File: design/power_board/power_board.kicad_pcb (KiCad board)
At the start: 2 copper layers, 68.5 x 38.5 mm, 48 parts, among them J1 Screw_Terminal_01x02, J2 Screw_Terminal_01x02, J3 Screw_Terminal_01x03, U1 LMR14050, U2 LT3045-1, U3 LT3045-1

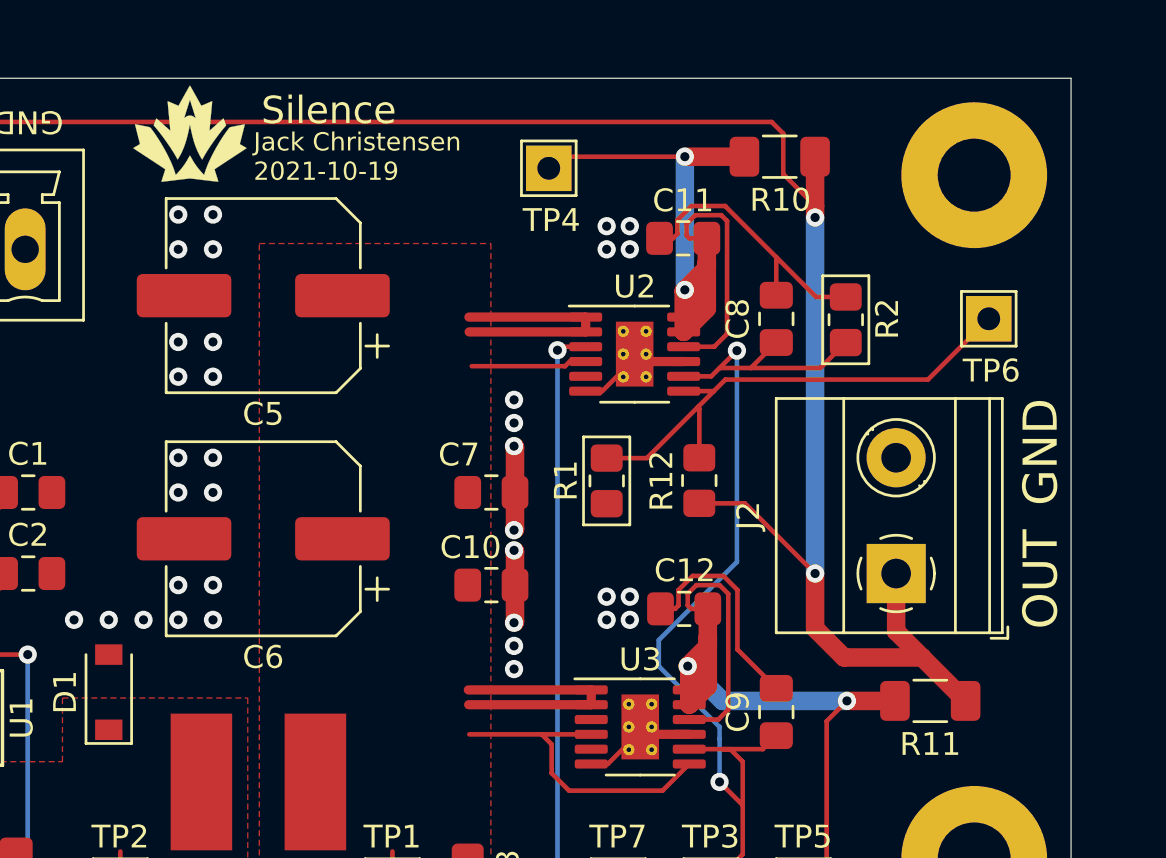
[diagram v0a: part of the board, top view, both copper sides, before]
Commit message: Address review comments, regenerate gerbers
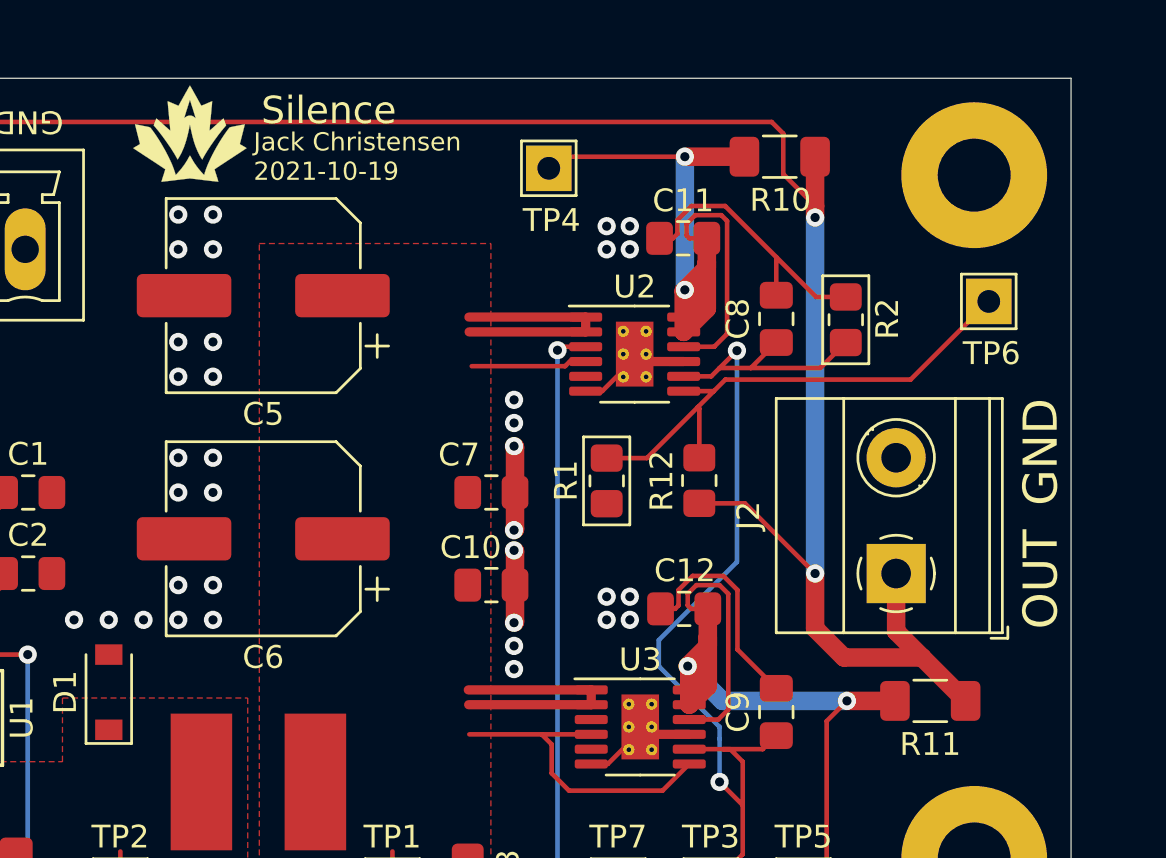
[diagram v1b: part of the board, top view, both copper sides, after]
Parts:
- moved TP6 0.76 mm to (167.6, 97.8)

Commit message: Update pdf, pcb
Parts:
- C3: value 10nF 16V -> 100nF 16V
- U1: value LMR14050 -> LMR14030

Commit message: Daq power board (#22)
* Create power_board2

* Add files via upload

* Add files via upload

* Delete design/power_board2

* Create keep

* Update and rename design/buck_converter_new.kicad_sch to design/power_board_2/buck_converter_new.kicad_sch

* Update and rename design/ldo_new.kicad_sch to design/power_board_2/ldo_new.kicad_sch

* Update and rename design/power_board_new.kicad_sch to design/power_board_2/power_board_new.kicad_sch

* Add files via upload

* Delete design/power_board/ldo.kicad_sch

* Add files via upload

* Add files via upload

* Add files via upload

* Add files via upload

* Delete design/power_board_2 directory

* Add files via upload

* Delete design/power_board/buck_fixed.sch

* Delete design/power_board/ldo.sch

* Delete design/power_board/power_board.sch

* Add files via upload

* Delete design/power_board/buck_fb.sch

* Update power_board.kicad_sch

* Add files via upload

* Add files via upload

* Add files via upload

* Add files via upload

* Changed footprint
Changed footprint path
changed footprint
Edit
Edit
Edit

* Edited calculations

* Added capacitor, switched input to right side`

* i

* Renamed file

* Added file

* Changed layout of ldo

* Changed filename to buck

* Added LED

* Changed diode footprints

* Updated LED calculations, diodes, LDO symbol

* Inductor footprint

* Updated buck diode

* shifted ldo schematic

* recent edits

* board layout

* edited layout

* rounded corners

* Moved capacitors up

* changed name of board

* Added logo and aligned J2 and J1

* routing

* altered trace width

---------

Co-authored-by: Aishwin Varghese <116891651+aishwin-varghese@users.noreply.github.com>
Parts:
- removed C10: OPT, Capacitor_SMD:C_0805_2012Metric_Pad1.18x1.45mm_HandSolder
- removed C11, C12: 10uF 35V, Capacitor_SMD:C_0805_2012Metric_Pad1.18x1.45mm_HandSolder
- removed C9: 4.7uF 35V, Capacitor_SMD:C_0805_2012Metric_Pad1.18x1.45mm_HandSolder
- removed the G*** at (132.6, 90.4)
- removed R11: 20mR, Resistor_SMD:R_1206_3216Metric_Pad1.30x1.75mm_HandSolder
- removed R12: 442k, Resistor_SMD:R_0805_2012Metric_Pad1.20x1.40mm_HandSolder
- removed R13: 38.3k, Resistor_SMD:R_0805_2012Metric_Pad1.20x1.40mm_HandSolder
- removed R14: 3.16k, Resistor_SMD:R_0805_2012Metric_Pad1.20x1.40mm_HandSolder
- removed R15: 1.91k, Resistor_SMD:R_0805_2012Metric_Pad1.20x1.40mm_HandSolder
- removed the REF** at (167.0, 92.2)
- removed the REF** at (167.0, 122.2)
- removed the REF** at (107.0, 122.2)
- removed the REF** at (107.0, 92.2)
- removed TP2, TP3, TP4, TP5, TP6, TP7, TP8: TestPoint, TestPoint:TestPoint_THTPad_2.0x2.0mm_Drill1.0mm
- removed U2: LT3045-1, Package_SO:MSOP-12-1EP_3x4mm_P0.65mm_EP1.65x2.85mm_ThermalVias
- added D2: B130-E3/5AT, Diode_SMD:D_SMA, F.Cu at (132.3, 109.5)
- added D4: LED, Diode_SMD:D_1206_3216Metric_Pad1.42x1.75mm_HandSolder, F.Cu at (157.4, 95.3)
- added D5: US1A, Diode_SMD:D_SMA, F.Cu at (135.9, 102.2)
- added G***: LOGO, rlcs:rocketry_logo_small, F.Cu at (159.0, 119.9)
- added REF**: MountingHole_3.2mm_M3_Pad, MountingHole:MountingHole_3.2mm_M3_Pad, F.Cu at (167.3, 121.2)
- added REF**: MountingHole_3.2mm_M3_Pad, MountingHole:MountingHole_3.2mm_M3_Pad, F.Cu at (107.3, 121.1)
- added REF**: MountingHole_3.2mm_M3_Pad, MountingHole:MountingHole_3.2mm_M3_Pad, F.Cu at (107.1, 93.0)
- added REF**: MountingHole_3.2mm_M3_Pad, MountingHole:MountingHole_3.2mm_M3_Pad, F.Cu at (167.3, 93.1)
- C1: value OPT -> 10uF
- C2: value 10uF 50V -> 1uF
- C3: value 100nF 16V -> 20uF
- C4: value 100nF 50V -> 10uF
- C5: value 39uF 35V -> 0.1uF; footprint Capacitor_SMD:CP_Elec_8x6.9 -> Capacitor_SMD:C_0805_2012Metric_Pad1.18x1.45mm_HandSolder
- C6: value 39uF 35V -> 10uF; footprint Capacitor_SMD:CP_Elec_8x6.9 -> Capacitor_SMD:C_0805_2012Metric_Pad1.18x1.45mm_HandSolder
- C7: value 10uF 35V -> 1uF
- C8: value 4.7uF 35V -> 10uF
- D1: value FSV360FP -> US1A; footprint Diode_SMD:D_SOD-123 -> Diode_SMD:D_SMA
- L1: value 15uH -> 22uH; footprint footprints:SRN6045 -> Inductor_SMD:L_Bourns-SRU1028_10.0x10.0mm
- R1: value 12.7k -> 20k
- R10: value 20mR -> _k; footprint Resistor_SMD:R_1206_3216Metric_Pad1.30x1.75mm_HandSolder -> Resistor_SMD:R_0805_2012Metric_Pad1.20x1.40mm_HandSolder
- R2: value 60.4k -> 10k
- R5: value 20k -> 100k
- R6: value 10k -> 277.58k
- R7: value 28k -> 10k
- R8: value 1.82k -> 240R
- R9: value 13.7k -> _k
- U1: value LMR14030 -> LV2862YDDCR; footprint Package_SO:TI_SO-PowerPAD-8 -> Package_TO_SOT_SMD:TSOT-23-6_HandSoldering
- U3: value LT3045-1 -> LM317MDCYR; footprint Package_SO:MSOP-12-1EP_3x4mm_P0.65mm_EP1.65x2.85mm_ThermalVias -> Package_TO_SOT_SMD:SOT-223-3_TabPin2
- moved R2 42.0 mm to (119.7, 103.9), turned to 180 degrees
- moved R9 36.9 mm to (152.4, 93.3), turned to 0 degrees
- moved R4 30.9 mm to (131.6, 96.8), turned to 90 degrees
- moved R8 28.8 mm to (146.6, 93.4)
- moved R5 27.0 mm to (125.2, 122.0), turned to -90 degrees
- moved TP1 26.9 mm to (136.3, 97.1)
- moved R1 25.6 mm to (125.6, 110.1), turned to 0 degrees
- moved C4 24.0 mm to (147.2, 113.8), turned to 0 degrees
- moved C5 23.9 mm to (147.1, 118.5), turned to 0 degrees
- moved R6 20.3 mm to (115.3, 117.2), turned to -90 degrees
- moved R3 18.3 mm to (125.6, 103.9)
- moved C6 18.3 mm to (153.2, 113.8), turned to 0 degrees
- moved R7 16.2 mm to (115.4, 121.9), turned to 90 degrees
- moved C7 14.3 mm to (153.1, 118.5)
- moved C3 12.9 mm to (119.8, 110.1), turned to 180 degrees
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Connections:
- C2 pad 1: +BATT -> Net-(D2-K)
- C2 pad 2: GND -> Net-(U1-CB)
- C3 pad 1: Net-(C3-Pad1) -> /buck/VOUT
- C4 pad 1: Net-(C4-Pad1) -> /buck/VOUT
- C4 pad 2: Net-(C4-Pad2) -> GND
- C5 pad 1: /ldo/VIN -> /buck/VOUT
- C6 pad 1: /ldo/VIN -> +OUT
- C7 pad 1: /ldo/VIN -> +OUT
- C8 pad 1: /ldo/SET -> GND
- C8 pad 2: GND -> Net-(D1-A)
- D1 pad 1: Net-(C4-Pad1) -> +OUT
- D1 pad 2: GND -> Net-(D1-A)
- J3 pad 1: Net-(J3-Pad1) -> Net-(J3-Pin_1)
- J3 pad 2: Net-(J3-Pad2) -> Net-(J3-Pin_2)
- L1 pad 1: Net-(C4-Pad1) -> Net-(D2-K)
- L1 pad 2: /ldo/VIN -> /buck/VOUT
- R1 pad 1: /ldo/SETFS -> Net-(J3-Pin_2)
- R1 pad 2: GND -> +BATT
- R10 pad 1: Net-(C11-Pad1) -> +OUT
- R10 pad 2: +OUT -> Net-(D4-A)
- R2 pad 1: /ldo/SET -> Net-(J3-Pin_2)
- R3 pad 1: Net-(J3-Pad2) -> Net-(J3-Pin_1)
- R3 pad 2: +BATT -> +OUT
- R4 pad 1: Net-(J3-Pad2) -> Net-(J3-Pin_1)
- R5 pad 1: Net-(J3-Pad1) -> +BATT
- R5 pad 2: +OUT -> Net-(U1-SHDN_N)
- R6 pad 1: Net-(J3-Pad1) -> /buck/VOUT
- R6 pad 2: GND -> Net-(U1-FB)
- R7 pad 1: +BATT -> Net-(U1-FB)
- R7 pad 2: Net-(R7-Pad2) -> GND
- R8 pad 1: GND -> Net-(D1-A)
- R8 pad 2: Net-(R7-Pad2) -> +OUT
- R9 pad 1: Net-(R9-Pad1) -> Net-(D1-A)
- TP1 pad 1: /ldo/VIN -> /buck/VOUT
- U1 pad 1: Net-(C4-Pad2) -> Net-(U1-CB)
- U1 pad 2: +BATT -> GND
- U1 pad 3: Net-(R7-Pad2) -> Net-(U1-FB)
- U1 pad 4: Net-(R9-Pad1) -> Net-(U1-SHDN_N)
- U1 pad 5: /buck/FB -> +BATT
- U1 pad 6: Net-(C3-Pad1) -> Net-(D2-K)
- U3 pad 1: /ldo/VIN -> Net-(D1-A)
- U3 pad 2: /ldo/VIN -> +OUT
- U3 pad 3: Net-(U3-Pad3) -> /buck/VOUT
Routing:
- net /buck/VOUT: track 0.00 -> 70.1 mm, vias 0 -> 2
- net /ldo/VIOC: track 63.6 -> 0.00 mm, vias 2 -> 0
- net /ldo/SET: track 44.4 -> 0.00 mm, vias 2 -> 0
- net /ldo/VIN: track 43.0 -> 0.00 mm
- net GND: track 39.9 -> 0.00 mm, vias 38 -> 0
- net Net-(C12-Pad1): track 38.2 -> 0.00 mm, vias 2 -> 0
- net Net-(C11-Pad1): track 34.7 -> 0.00 mm, vias 2 -> 0
- net Net-(J3-Pad2): track 33.5 -> 0.00 mm
- net Net-(J3-Pin_2): track 0.00 -> 31.4 mm, vias 0 -> 2
- net Net-(D1-A): track 0.00 -> 28.2 mm
- net /ldo/SETFS: track 23.2 -> 0.00 mm
- net Net-(D2-K): track 0.00 -> 22.1 mm
- net Net-(J3-Pin_1): track 0.00 -> 21.1 mm
- net +OUT: track 96.4 -> 77.4 mm, vias 2 -> 0
- net Net-(J3-Pad1): track 17.3 -> 0.00 mm
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- added copper zone on B.Cu, net +BATT
- removed copper zone on F.Cu, net /ldo/VIN
- removed copper zone on B.Cu, net GND
- removed copper zone on F.Cu, net Net-(C4-Pad1)
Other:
- board size 68.5 x 38.5 mm -> 68.5 x 36.5 mm
- net class Default removed
- board text added: "Anastasia Vassos 2024-02-13"
- board text added: "DAQ Power"
- board text removed: "Jack Christensen 2021-10-19"
- board text removed: "Silence"
